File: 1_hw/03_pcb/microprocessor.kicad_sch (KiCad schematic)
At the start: 31 parts, among them U3 STM32F446ZETx, Y2 32.768k

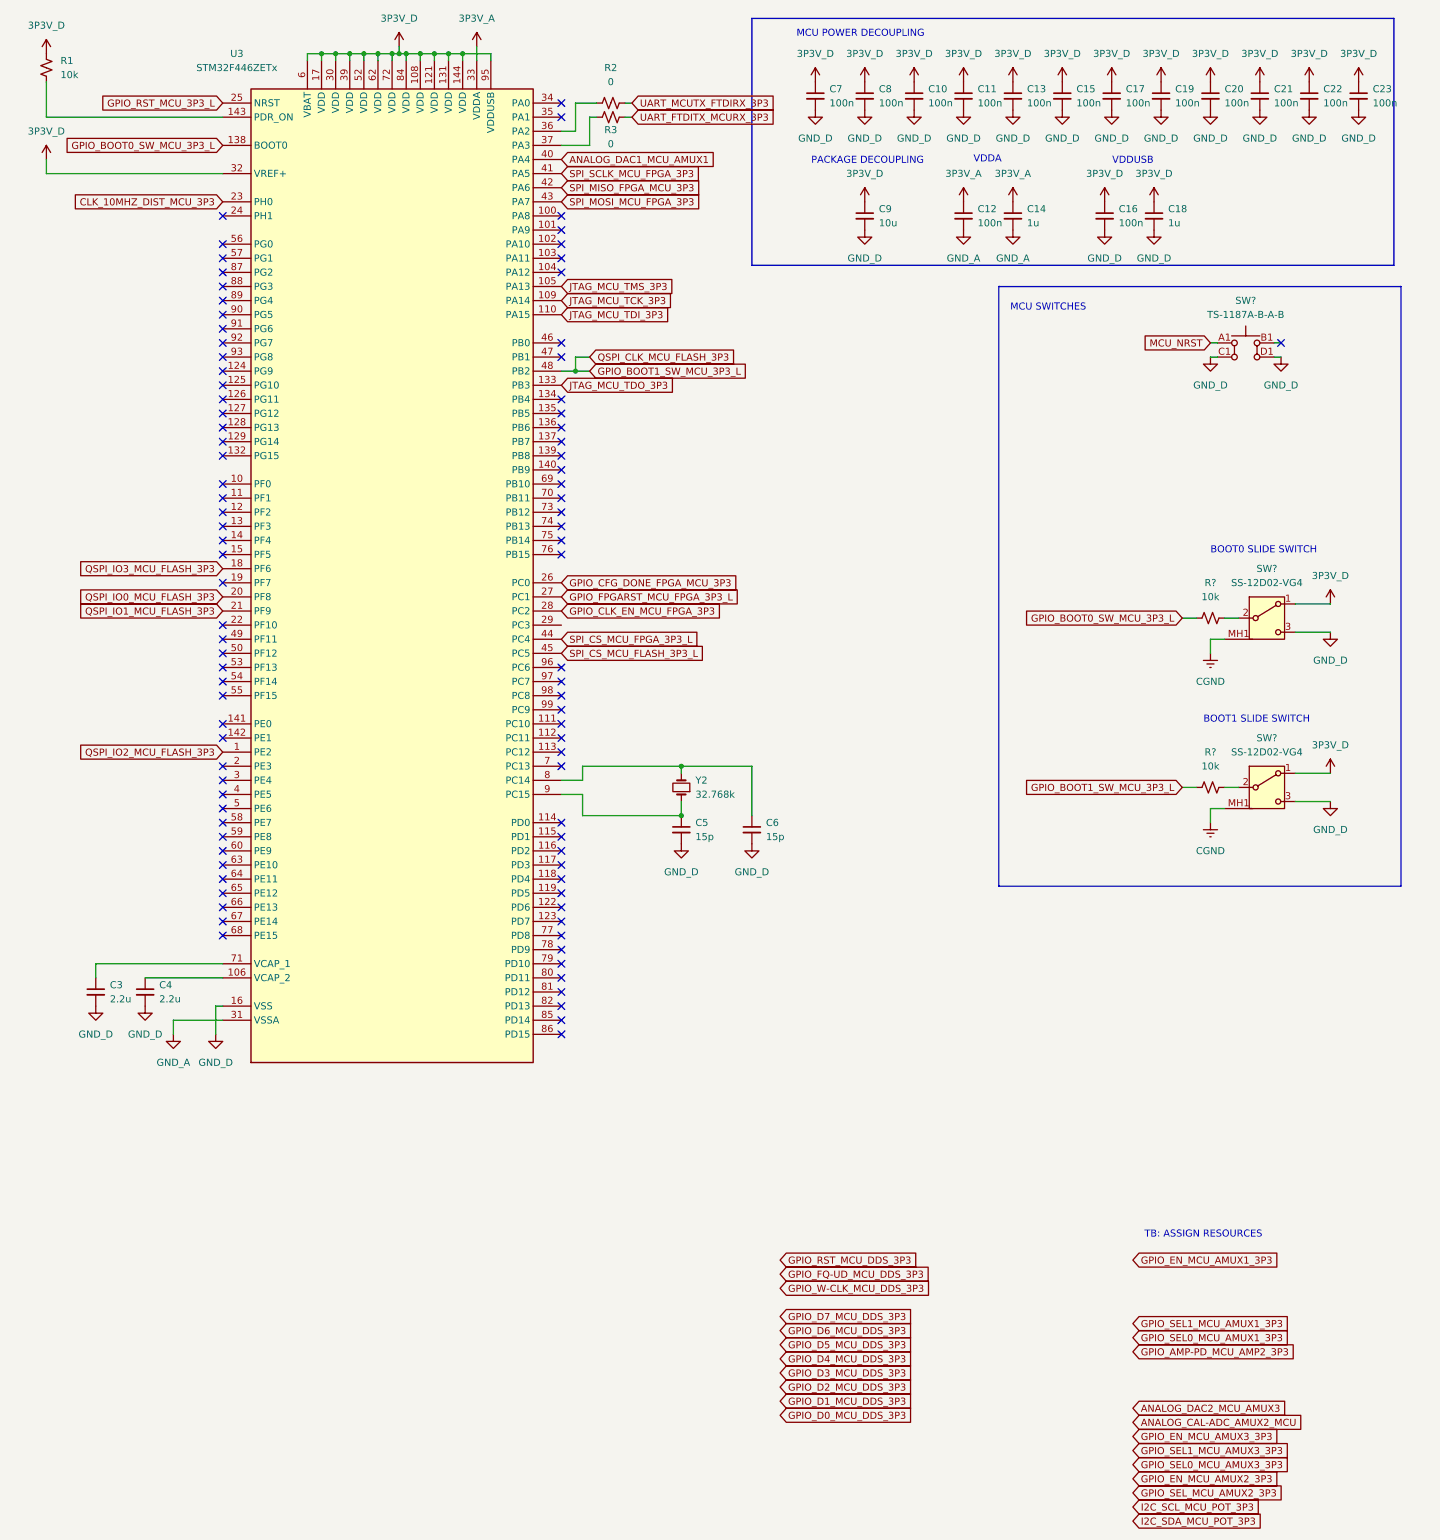
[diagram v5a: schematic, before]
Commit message: FEAT: Added MCU Resources for Analog Muxing, Additional DAC, ADC, and I2C for Digital Pot. Also changed SPI Resource from 1 to 2.
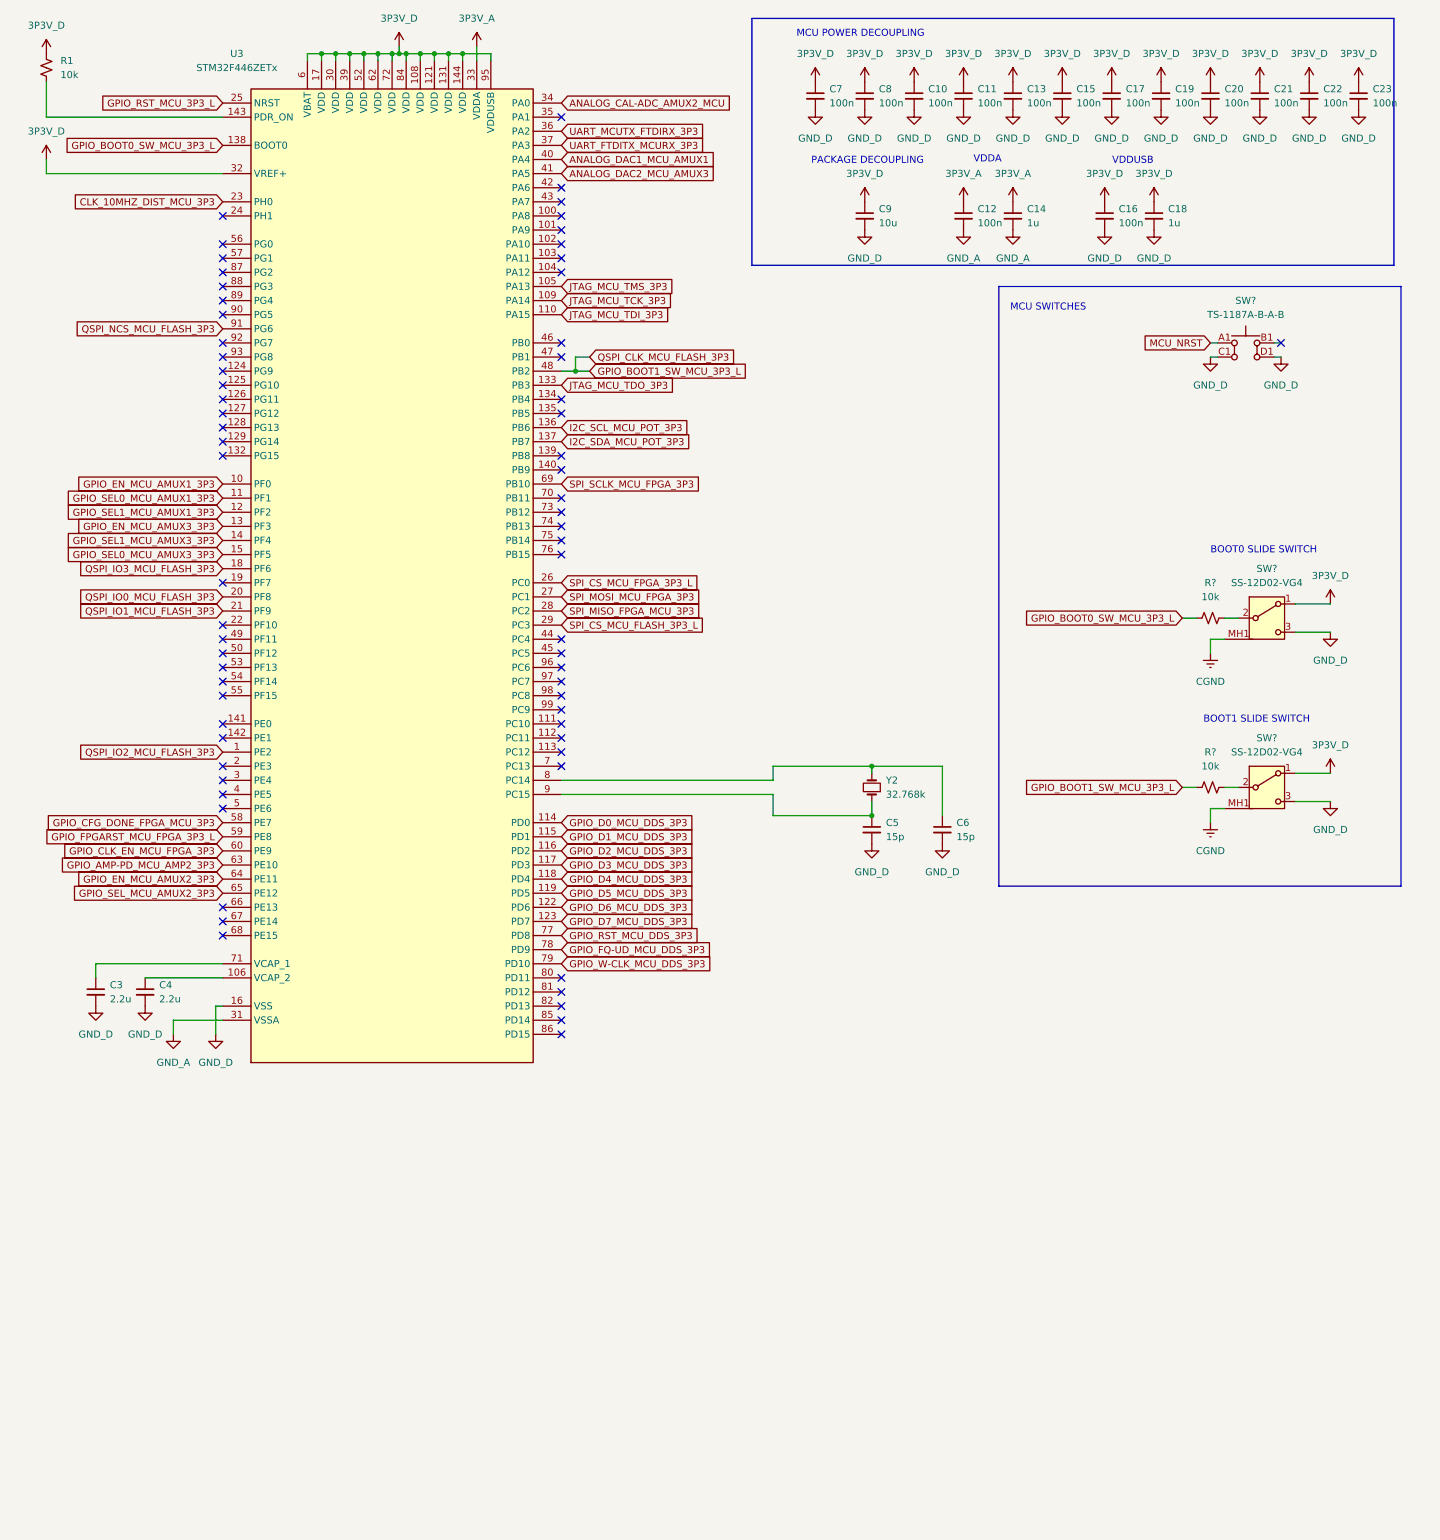
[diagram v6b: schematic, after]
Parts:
- removed R2, R3: 0, Resistor_SMD:R_0603_1608Metric, symbol Device:R_Small_US
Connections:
- net ANALOG_CAL-ADC_AMUX2_MCU: now also U3.34 (PA0)
- net ANALOG_DAC2_MCU_AMUX3: now also U3.41 (PA5)
- net GPIO_AMP-PD_MCU_AMP2_3P3: now also U3.63 (PE10)
- net GPIO_CFG_DONE_FPGA_MCU_3P3: now also U3.58 (PE7); no longer U3.26 (PC0)
- net GPIO_CLK_EN_MCU_FPGA_3P3: now also U3.60 (PE9); no longer U3.28 (PC2)
- net GPIO_D0_MCU_DDS_3P3: now also U3.114 (PD0)
- net GPIO_D1_MCU_DDS_3P3: now also U3.115 (PD1)
- net GPIO_D2_MCU_DDS_3P3: now also U3.116 (PD2)
- net GPIO_D3_MCU_DDS_3P3: now also U3.117 (PD3)
- net GPIO_D4_MCU_DDS_3P3: now also U3.118 (PD4)
- net GPIO_D5_MCU_DDS_3P3: now also U3.119 (PD5)
- net GPIO_D6_MCU_DDS_3P3: now also U3.122 (PD6)
- net GPIO_D7_MCU_DDS_3P3: now also U3.123 (PD7)
- net GPIO_EN_MCU_AMUX1_3P3: now also U3.10 (PF0)
- net GPIO_EN_MCU_AMUX2_3P3: now also U3.64 (PE11)
- net GPIO_EN_MCU_AMUX3_3P3: now also U3.13 (PF3)
- net GPIO_FPGARST_MCU_FPGA_3P3_L: now also U3.59 (PE8); no longer U3.27 (PC1)
- net GPIO_FQ-UD_MCU_DDS_3P3: now also U3.78 (PD9)
- net GPIO_RST_MCU_DDS_3P3: now also U3.77 (PD8)
- net GPIO_SEL0_MCU_AMUX1_3P3: now also U3.11 (PF1)
- net GPIO_SEL0_MCU_AMUX3_3P3: now also U3.15 (PF5)
- net GPIO_SEL1_MCU_AMUX1_3P3: now also U3.12 (PF2)
- net GPIO_SEL1_MCU_AMUX3_3P3: now also U3.14 (PF4)
- net GPIO_SEL_MCU_AMUX2_3P3: now also U3.65 (PE12)
- net GPIO_W-CLK_MCU_DDS_3P3: now also U3.79 (PD10)
- net I2C_SCL_MCU_POT_3P3: now also U3.136 (PB6)
- net I2C_SDA_MCU_POT_3P3: now also U3.137 (PB7)
- net SPI_CS_MCU_FLASH_3P3_L: now also U3.29 (PC3); no longer U3.45 (PC5)
- net SPI_CS_MCU_FPGA_3P3_L: now also U3.26 (PC0); no longer U3.44 (PC4)
- net SPI_MISO_FPGA_MCU_3P3: now also U3.28 (PC2); no longer U3.42 (PA6)
- net SPI_MOSI_MCU_FPGA_3P3: now also U3.27 (PC1); no longer U3.43 (PA7)
- net SPI_SCLK_MCU_FPGA_3P3: now also U3.69 (PB10); no longer U3.41 (PA5)
- net UART_FTDITX_MCURX_3P3: now also U3.37 (PA3)
- net UART_MCUTX_FTDIRX_3P3: now also U3.36 (PA2)
- net QSPI_NCS_MCU_FLASH_3P3: now reaches U3.91 (PG6)
- no-connect marks 91 -> 67
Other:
- note removed: "TB: ASSIGN RESOURCES"
- moved on the sheet: C5, C6, Y2

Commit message: FEAT: Changed from two grounds (Digital + Analog) to Singular Ground IAW recommended Grounding Scheme.
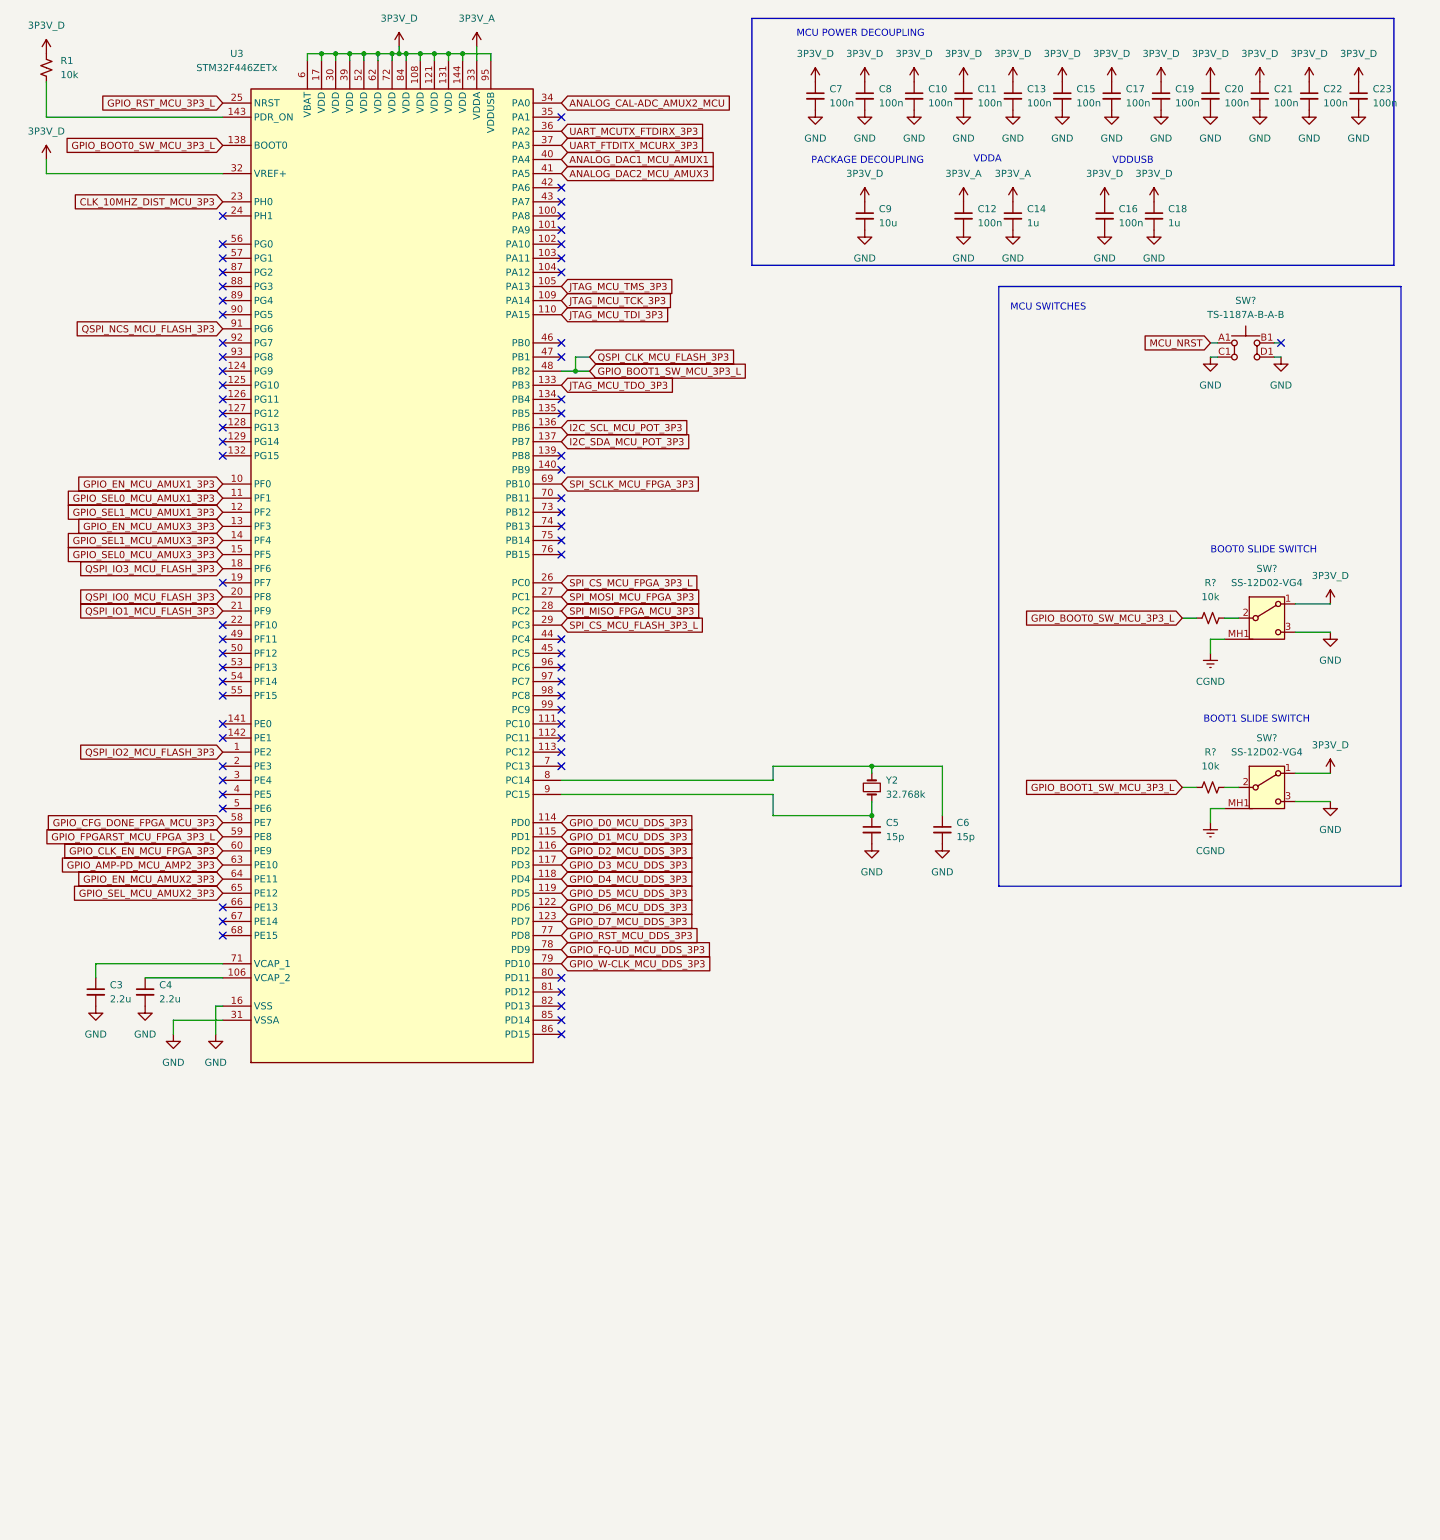
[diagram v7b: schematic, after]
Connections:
- net GND_D is gone; now on net GND: C10.2, C11.2, C13.2, C15.2, C16.2, C17.2, C18.2, C19.2, C20.2, C21.2, C22.2, C23.2, C3.2, C4.2, C5.2, C6.2, C7.2, C8.2, C9.2, SW?.3 (NO), SW?.3 (NO), SW?.C1 (NO_1), SW?.D1 (NO_2), U3.107 (VSS), U3.120 (VSS), U3.130 (VSS), U3.16 (VSS), U3.38 (VSS), U3.51 (VSS), U3.61 (VSS), U3.83 (VSS), U3.94 (VSS)
- net GND_A renamed GND
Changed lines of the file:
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@@
 			)
 		)
-		(property "Value" "GND_D"
+		(property "Value" "GND"
 			(at 207.01 57.15 0)
 			(effects
@@
 			)
 		)
-		(property "Value" "GND_D"
+		(property "Value" "GND"
 			(at 247.65 129.54 0)
 			(effects
@@
 			)
 		)
-		(property "Value" "GND_D"
+		(property "Value" "GND"
 			(at 177.8 167.64 0)
 			(effects
@@
 			)
 		)
-		(property "Value" "GND_D"
+		(property "Value" "GND"
 			(at 199.39 35.56 0)
 			(effects
@@
 			)
 		)
-		(property "Value" "GND_D"
+		(property "Value" "GND"
 			(at 217.17 35.56 0)
 			(effects
@@
 			)
 		)
-		(property "Value" "GND_D"
+		(property "Value" "GND"
 			(at 154.94 35.56 0)
 			(effects
@@
 			)
 		)
-		(property "Value" "GND_D"
+		(property "Value" "GND"
 			(at 247.65 160.02 0)
 			(effects
@@
 			)
 		)
-		(property "Value" "GND_D"
+		(property "Value" "GND"
 			(at 172.72 35.56 0)
 			(effects
@@
 			)
 		)
-		(property "Value" "GND_D"
+		(property "Value" "GND"
 			(at 226.06 80.01 0)
 			(effects
@@
 			)
 		)
-		(property "Value" "GND_A"
+		(property "Value" "GND"
 			(at 39.37 201.93 0)
 			(effects
@@
 			)
 		)
-		(property "Value" "GND_D"
+		(property "Value" "GND"
 			(at 243.84 35.56 0)
 			(effects
@@
 			)
 		)
-		(property "Value" "GND_D"
+		(property "Value" "GND"
 			(at 165.1 167.64 0)
 			(effects
@@
 			)
 		)
-		(property "Value" "GND_D"
+		(property "Value" "GND"
 			(at 215.9 57.15 0)
 			(effects
@@
 			)
 		)
-		(property "Value" "GND_D"
+		(property "Value" "GND"
 			(at 163.83 35.56 0)
 			(effects
@@
 			)
 		)
-		(property "Value" "GND_D"
+		(property "Value" "GND"
 			(at 34.29 196.85 0)
 			(effects
@@
 			)
 		)
-		(property "Value" "GND_D"
+		(property "Value" "GND"
 			(at 163.83 57.15 0)
 			(effects
@@
 			)
 		)
-		(property "Value" "GND_D"
+		(property "Value" "GND"
 			(at 226.06 35.56 0)
 			(effects
@@
 			)
 		)
-		(property "Value" "GND_A"
+		(property "Value" "GND"
 			(at 181.61 57.15 0)
 			(effects
@@
 			)
 		)
-		(property "Value" "GND_D"
+		(property "Value" "GND"
 			(at 234.95 35.56 0)
 			(effects
@@
 			)
 		)
-		(property "Value" "GND_D"
+		(property "Value" "GND"
 			(at 46.99 201.93 0)
 			(effects
@@
 			)
 		)
-		(property "Value" "GND_D"
+		(property "Value" "GND"
 			(at 238.76 80.01 0)
 			(effects
@@
 			)
 		)
-		(property "Value" "GND_D"
+		(property "Value" "GND"
 			(at 181.61 35.56 0)
 			(effects
@@
 			)
 		)
-		(property "Value" "GND_D"
+		(property "Value" "GND"
 			(at 190.5 35.56 0)
 			(effects
@@
 			)
 		)
-		(property "Value" "GND_D"
+		(property "Value" "GND"
 			(at 25.4 196.85 0)
 			(effects
@@
 			)
 		)
-		(property "Value" "GND_D"
+		(property "Value" "GND"
 			(at 252.73 35.56 0)
 			(effects
@@
 			)
 		)
-		(property "Value" "GND_D"
+		(property "Value" "GND"
 			(at 208.28 35.56 0)
 			(effects
@@
 			)
 		)
-		(property "Value" "GND_A"
+		(property "Value" "GND"
 			(at 190.5 57.15 0)
 			(effects

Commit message: FEAT: Added +15V and -15V Regulator. Replaced some Symbols to add additional Part Number Field.
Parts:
- SW? (x2): footprint (none) -> BRZK_TBD; Part Number (none) -> SS-12D02-VG4
- SW?: footprint TS1187ABAB -> BRZK_TBD; Part Number (none) -> TS-1187A-B-A-B
- U3: Part Number (none) -> STM32F446ZET7
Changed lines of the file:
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@@
 			)
 		)
-		(property "Footprint" ""
+		(property "Footprint" "BRZK_TBD"
 			(at 236.22 152.4 0)
 			(effects
@@
 			)
 		)
+		(property "Part Number" "SS-12D02-VG4"
+			(at 236.22 152.4 0)
+			(effects
+				(font
+					(size 1.27 1.27)
+				)
+				(hide yes)
+			)
+		)
 		(pin "3"
 		)
@@
 			)
 		)
+		(property "Part Number" "STM32F446ZET7"
+			(at 78.74 115.57 0)
+			(effects
+				(font
+					(size 1.27 1.27)
+				)
+				(hide yes)
+			)
+		)
 		(pin "129"
 		)
@@
 			)
 		)
-		(property "Footprint" ""
+		(property "Footprint" "BRZK_TBD"
 			(at 236.22 121.92 0)
 			(effects
@@
 			)
 		)
+		(property "Part Number" "SS-12D02-VG4"
+			(at 236.22 121.92 0)
+			(effects
+				(font
+					(size 1.27 1.27)
+				)
+				(hide yes)
+			)
+		)
 		(pin "3"
 		)
@@
 			)
 		)
-		(property "Footprint" "TS1187ABAB"
+		(property "Footprint" "BRZK_TBD"
 			(at 232.41 67.31 0)
 			(effects
@@
 			(effects
 				(font
+					(size 1.27 1.27)
+				)
+				(hide yes)
+			)
+		)
+		(property "Part Number" "TS-1187A-B-A-B"
+			(at 232.41 73.66 0)
+			(effects
+				(font
